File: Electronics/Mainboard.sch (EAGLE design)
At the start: 35 parts, among them IC1 4081N, IC2 4069N, Q1 IRFZ48V, Q2 IRF4905V, Q3 IRFZ48V, Q4 IRF4905V, Q5 IRFZ48V, Q6 IRF4905V, Q7 IRFZ48V, Q8 IRF4905V, X3 24V Batt

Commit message: Arduino sofware, updated electronics and some report outline.
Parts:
- removed C1: (no value), rcl:CPOL-EUE7.5-18
- added C2: (no value), rcl:CPOL-EUE5-10.5
- added LED1: (no value), led:LED5MM
- added R13: 1k, rcl:R-EU_0207/10
- R10, R11, R12, R7, R8, R9: value (none) -> 180
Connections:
- net N$35 renamed +3V3
- removed net N$29: C1.-, OK1.EMIT, OK2.EMIT, OK3.EMIT, OK4.EMIT, OK5.EMIT, OK6.EMIT, Q1.S, Q3.S, Q5.S, Q7.S, X3-2.KL
- removed net N$30: C1.+, Q2.S, Q4.S, Q6.S, Q8.S, R1.2, R2.2, R3.2, R4.2, R5.2, R6.2, X3-1.KL
- new net +24V: C2.+, LED1.A, Q2.S, Q4.S, Q6.S, Q8.S, R1.2, R2.2, R3.2, R4.2, R5.2, R6.2, X3-1.KL
- new net GND2: C2.-, OK1.EMIT, OK2.EMIT, OK3.EMIT, OK4.EMIT, OK5.EMIT, OK6.EMIT, Q1.S, Q3.S, Q5.S, Q7.S, R13.1, X3-2.KL
- new net N$41: JP1.3
- new net N$42: JP1.4
- new net N$6: LED1.C, R13.2
- net N$26: no longer JP1.4
- net N$37: no longer JP1.3
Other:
- note added: "Beskyttelses dioder?"
- note added: "Level Shifter"
- moved on the sheet: JP1, X3-1, X3-2

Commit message: 
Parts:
- removed C2: (no value), rcl:CPOL-EUE5-10.5
- removed IC2: 4069N, 40xx:4069N
- removed LED1: (no value), led:LED5MM
- removed OK1, OK2, OK3, OK4, OK5, OK6: PC817, optocoupler:PC817
- removed Q1, Q3, Q5, Q7: IRFZ48V, transistor-power:IRFZ48V
- removed Q2, Q4, Q6, Q8: IRF4905V, transistor-power:IRF4905V
- removed R1, R2, R3, R4, R5, R6: 10k, rcl:R-EU_0207/10
- removed R11, R12: 180, rcl:R-EU_0207/10
- removed R13: 1k, rcl:R-EU_0207/10
- removed X1, X2: (no value), con-wago-508:W237-02P
- removed X3: 24V Batt, con-wago-508:W237-02P
- added JP2: Motorcontroller, pinhead:PINHD-2X5
- added JP5: Display, pinhead:PINHD-2X7
- added T1, T2: BC547, transistor:BC547
- JP1: device pinhead:PINHD-1X6 -> pinhead:PINHD-2X7
- R10, R9: value 180 -> 1k
- R7, R8: value 180 -> 10k
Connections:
- removed net +24V: C2.+, LED1.A, Q2.S, Q4.S, Q6.S, Q8.S, R1.2, R2.2, R3.2, R4.2, R5.2, R6.2, X3-1.KL
- removed net GND2: C2.-, OK1.EMIT, OK2.EMIT, OK3.EMIT, OK4.EMIT, OK5.EMIT, OK6.EMIT, Q1.S, Q3.S, Q5.S, Q7.S, R13.1, X3-2.KL
- removed net N$12: OK1.COL, Q1.G, Q2.G, R1.1
- removed net N$13: OK3.COL, Q3.G, R3.1
- removed net N$14: OK3.A, R9.2
- removed net N$15: IC1A.O, R8.1
- removed net N$18: Q7.D, Q8.D, X2-1.KL
- removed net N$19: OK4.COL, Q7.G, Q8.G, R4.1
- removed net N$21: OK5.COL, Q6.G, R5.1
- removed net N$22: OK6.COL, Q5.G, R6.1
- removed net N$23: OK6.A, R12.2
- removed net N$24: IC1C.O, R11.1
- removed net N$25: IC1D.O, R12.1
- removed net N$27: IC1D.I0, IC2B.I, R10.1, U$1.D4
- removed net N$28: OK1.A, R7.2
- removed net N$6: LED1.C, R13.2
- removed net N$9: OK2.COL, Q4.G, R2.1
- removed net VCC: IC1P.VDD, IC2P.VDD, U$1.5V
- new net +5V: IC1P.VDD, JP5.2, R7.2, R8.2, U$1.5V
- new net N$31: JP5.4, U$1.D6
- new net N$38: JP5.8, U$1.D8
- new net N$40: JP5.10, U$1.D9
- new net N$43: JP5.14, U$1.D11
- new net N$44: JP5.3, U$1.D12
- new net N$45: JP5.5, U$1.D13
- new net N$46: JP5.7, U$1.A3
- net GND: now also JP1.3, JP2.10, JP5.1, T1.E, T2.E; no longer IC2P.VSS, JP1.2, OK1.C, OK2.C, OK3.C, OK4.C, OK5.C, OK6.C
- net N$1: now also IC1A.O, JP2.2; no longer Q5.D, Q6.D, X2-2.KL
- net N$10: now also JP2.1, R9.1; no longer IC2A.I, R7.1
- net N$16: now also R8.1, T2.C; no longer IC2B.O
- net N$17: now also R9.2, T1.B; no longer IC1B.O, R9.1
- net N$2: now also IC1B.O, JP2.3; no longer Q3.D, Q4.D, X1-1.KL
- net N$20: now also R10.2, T2.B; no longer OK5.A, R11.2
- net N$26: now also JP1.7
- net N$3: now also IC1D.I0, JP2.4, R10.1, U$1.D4; no longer OK2.A, R8.2
- net N$37: now also JP5.6, U$1.D7; no longer U$1.A4
- net N$4: now also IC1C.O, JP2.5; no longer Q1.D, Q2.D, X1-2.KL
- net N$41: now also JP1.5, U$1.A4; no longer JP1.3
- net N$42: now also JP5.12, U$1.D10; no longer JP1.4
- net N$5: now also IC1D.O, JP2.6; no longer OK4.A, R10.2
- net N$8: now also R7.1, T1.C; no longer IC2A.O
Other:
- note removed: "Beskyttelses dioder?"
- note removed: "Level Shifter"
- moved on the sheet: IC1A, IC1B, IC1C, IC1D, IC1P, R10, R7, R8, R9

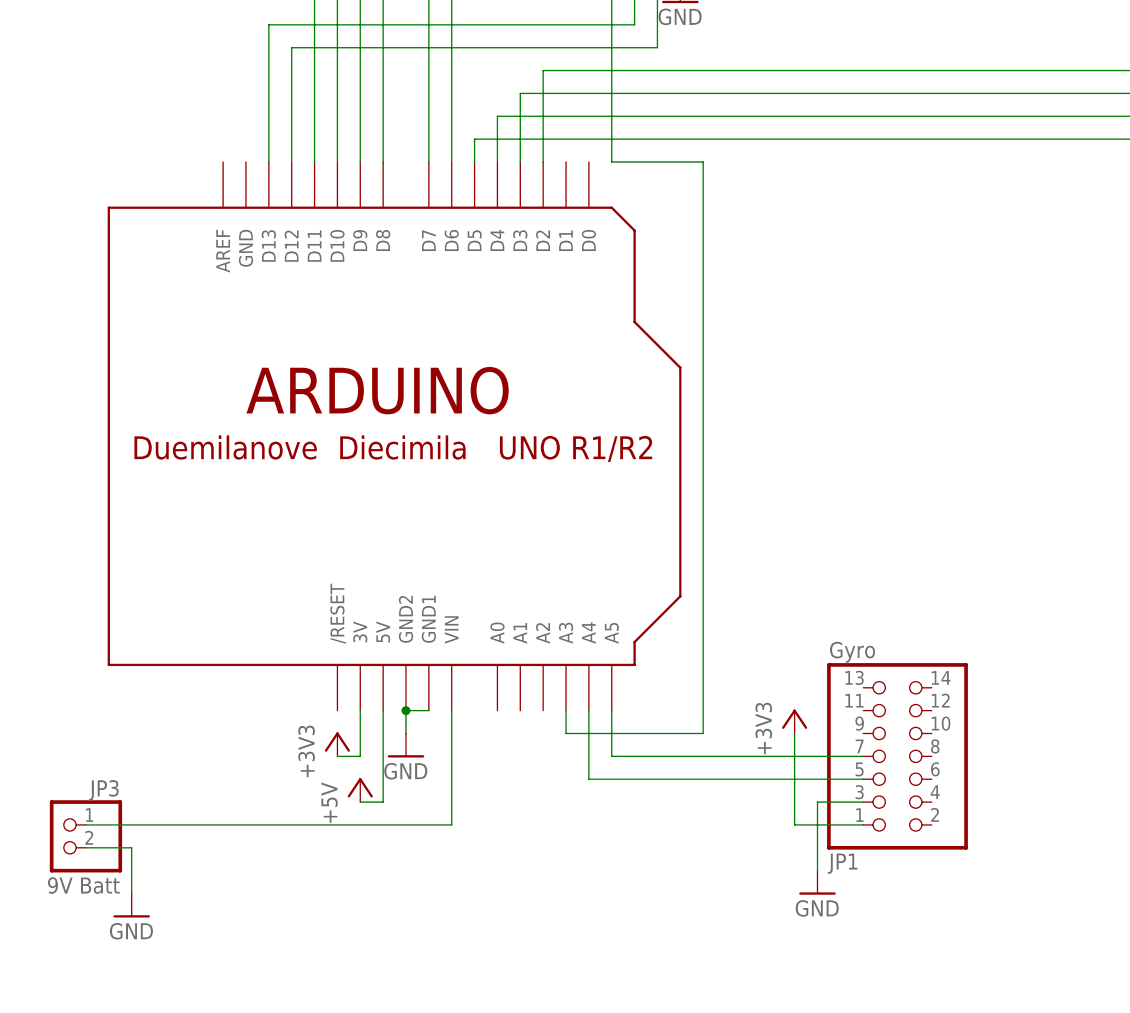
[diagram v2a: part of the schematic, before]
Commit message: Mainboard 2.0. Fixes #1, #2 #12
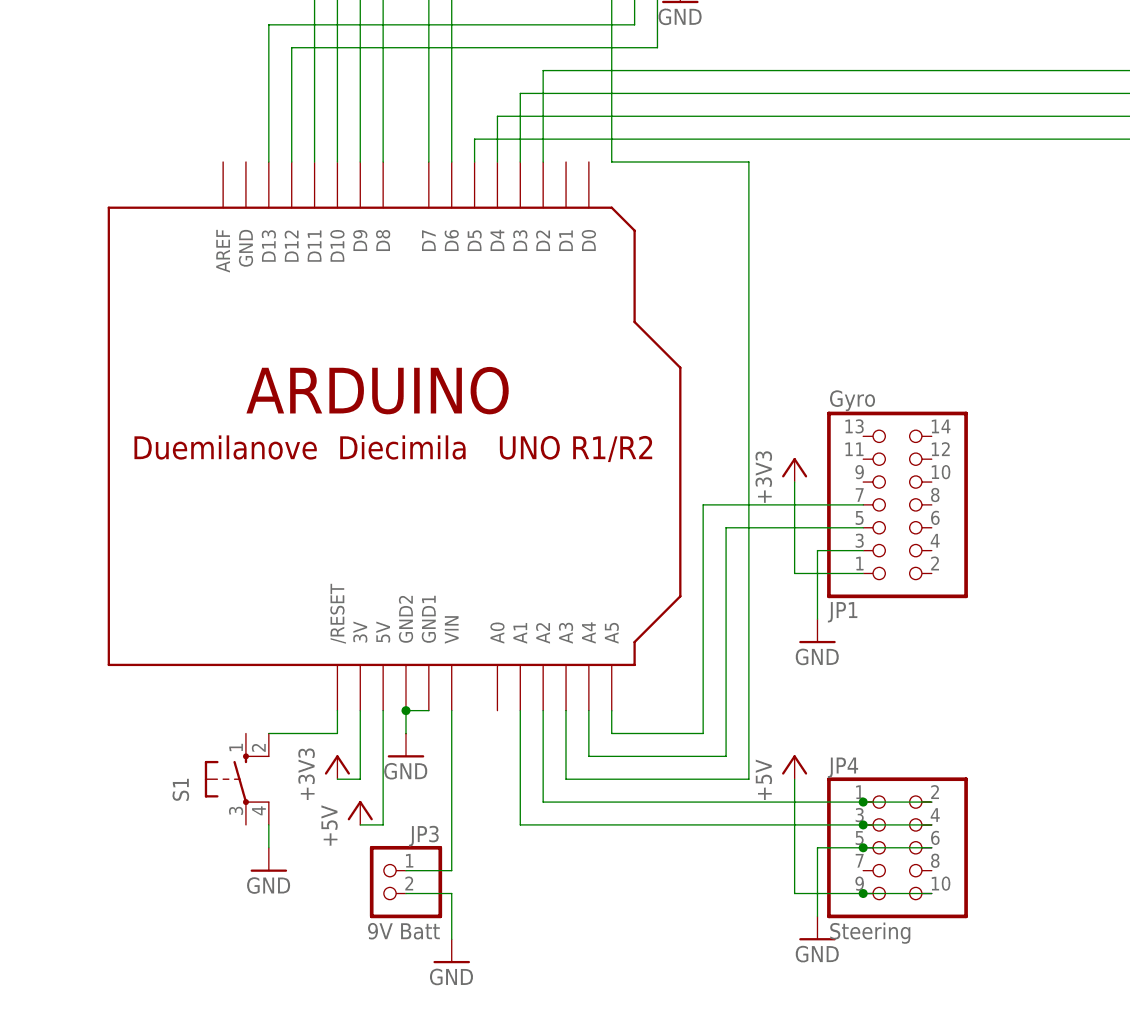
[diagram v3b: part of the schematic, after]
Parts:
- added JP4: Steering, pinhead:PINHD-2X5
- added S1: (no value), switch-omron:10-XX
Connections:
- new net N$13: JP4.3, JP4.4, U$1.A1
- new net N$14: JP4.1, JP4.2, U$1.A2
- new net N$15: S1.S1, U$1./RESET
- net +5V: now also JP4.10, JP4.9
- net GND: now also JP4.5, JP4.6, S1.P1
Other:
- moved on the sheet: JP1, JP3
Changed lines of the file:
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@@
 <?xml version="1.0" encoding="utf-8"?>
 <!DOCTYPE eagle SYSTEM "eagle.dtd">
-<eagle version="6.0">
+<eagle version="6.1">
 <drawing>
 <settings>
@@
 <part name="P+4" library="supply1" deviceset="+5V" device=""/>
 <part name="P+5" library="supply1" deviceset="+5V" device=""/>
+<part name="GND9" library="supply1" deviceset="GND" device=""/>
+<part name="P+6" library="supply1" deviceset="+5V" device=""/>
+<part name="JP4" library="pinhead" deviceset="PINHD-2X5" device="" value="Steering"/>
+<part name="S1" library="switch-omron" deviceset="10-XX" device=""/>
+<part name="GND10" library="supply1" deviceset="GND" device=""/>
 </parts>
 <sheets>
@@
 <instance part="IC1" gate="C" x="132.08" y="55.88"/>
 <instance part="IC1" gate="D" x="132.08" y="40.64"/>
-<instance part="JP1" gate="A" x="53.34" y="35.56" rot="MR180"/>
-<instance part="JP3" gate="G$1" x="-38.1" y="25.4" rot="MR0"/>
-<instance part="GND1" gate="1" x="-30.48" y="17.78"/>
-<instance part="GND2" gate="1" x="45.72" y="20.32"/>
+<instance part="JP1" gate="A" x="53.34" y="63.5" rot="MR180"/>
+<instance part="JP3" gate="G$1" x="-2.54" y="20.32" rot="MR0"/>
+<instance part="GND1" gate="1" x="5.08" y="12.7"/>
+<instance part="GND2" gate="1" x="45.72" y="48.26"/>
 <instance part="GND3" gate="1" x="0" y="35.56"/>
 <instance part="GND4" gate="1" x="91.44" y="27.94"/>
 <instance part="GND6" gate="1" x="162.56" y="68.58"/>
-<instance part="+3V1" gate="G$1" x="-7.62" y="38.1"/>
-<instance part="+3V2" gate="G$1" x="43.18" y="40.64"/>
+<instance part="+3V1" gate="G$1" x="-7.62" y="35.56"/>
+<instance part="+3V2" gate="G$1" x="43.18" y="68.58"/>
 <instance part="T1" gate="G$1" x="119.38" y="111.76"/>
 <instance part="T2" gate="G$1" x="116.84" y="58.42"/>
@@
 <instance part="P+3" gate="1" x="137.16" y="121.92"/>
 <instance part="P+4" gate="1" x="137.16" y="68.58"/>
-<instance part="P+5" gate="1" x="-5.08" y="33.02"/>
+<instance part="P+5" gate="1" x="-5.08" y="30.48"/>
+<instance part="GND9" gate="1" x="45.72" y="15.24"/>
+<instance part="P+6" gate="1" x="43.18" y="35.56"/>
+<instance part="JP4" gate="A" x="53.34" y="25.4"/>
+<instance part="S1" gate="1" x="-17.78" y="33.02"/>
+<instance part="GND10" gate="1" x="-15.24" y="22.86"/>
 </instances>
 <busses>
@@
 <segment>
 <pinref part="U$1" gate="G$1" pin="VIN"/>
-<wire x1="5.08" y1="40.64" x2="5.08" y2="27.94" width="0.1524" layer="91"/>
-<wire x1="5.08" y1="27.94" x2="-35.56" y2="27.94" width="0.1524" layer="91"/>
+<wire x1="5.08" y1="40.64" x2="5.08" y2="22.86" width="0.1524" layer="91"/>
+<wire x1="5.08" y1="22.86" x2="0" y2="22.86" width="0.1524" layer="91"/>
 <pinref part="JP3" gate="G$1" pin="1"/>
 </segment>
@@
 <pinref part="GND1" gate="1" pin="GND"/>
 <pinref part="JP3" gate="G$1" pin="2"/>
-<wire x1="-35.56" y1="25.4" x2="-30.48" y2="25.4" width="0.1524" layer="91"/>
-<wire x1="-30.48" y1="25.4" x2="-30.48" y2="20.32" width="0.1524" layer="91"/>
+<wire x1="0" y1="20.32" x2="5.08" y2="20.32" width="0.1524" layer="91"/>
+<wire x1="5.08" y1="20.32" x2="5.08" y2="15.24" width="0.1524" layer="91"/>
 </segment>
 <segment>
 <pinref part="JP1" gate="A" pin="3"/>
-<wire x1="50.8" y1="30.48" x2="45.72" y2="30.48" width="0.1524" layer="91"/>
-<wire x1="45.72" y1="30.48" x2="45.72" y2="22.86" width="0.1524" layer="91"/>
+<wire x1="50.8" y1="58.42" x2="45.72" y2="58.42" width="0.1524" layer="91"/>
+<wire x1="45.72" y1="58.42" x2="45.72" y2="50.8" width="0.1524" layer="91"/>
 <pinref part="GND2" gate="1" pin="GND"/>
 </segment>
@@
 <wire x1="30.48" y1="121.92" x2="30.48" y2="127" width="0.1524" layer="91"/>
 </segment>
+<segment>
+<wire x1="45.72" y1="25.4" x2="45.72" y2="17.78" width="0.1524" layer="91"/>
+<pinref part="GND9" gate="1" pin="GND"/>
+<pinref part="JP4" gate="A" pin="5"/>
+<wire x1="45.72" y1="25.4" x2="50.8" y2="25.4" width="0.1524" layer="91"/>
+<pinref part="JP4" gate="A" pin="6"/>
+<wire x1="50.8" y1="25.4" x2="58.42" y2="25.4" width="0.1524" layer="91"/>
+<junction x="50.8" y="25.4"/>
+</segment>
+<segment>
+<pinref part="GND10" gate="1" pin="GND"/>
+<pinref part="S1" gate="1" pin="P1"/>
+<wire x1="-15.24" y1="25.4" x2="-15.24" y2="27.94" width="0.1524" layer="91"/>
+</segment>
 </net>
 <net name="N$26" class="0">
 <segment>
 <pinref part="U$1" gate="G$1" pin="A5"/>
-<wire x1="22.86" y1="40.64" x2="22.86" y2="35.56" width="0.1524" layer="91"/>
+<wire x1="22.86" y1="40.64" x2="22.86" y2="38.1" width="0.1524" layer="91"/>
 <pinref part="JP1" gate="A" pin="7"/>
-<wire x1="50.8" y1="35.56" x2="22.86" y2="35.56" width="0.1524" layer="91"/>
+<wire x1="50.8" y1="63.5" x2="33.02" y2="63.5" width="0.1524" layer="91"/>
+<wire x1="33.02" y1="63.5" x2="33.02" y2="38.1" width="0.1524" layer="91"/>
+<wire x1="33.02" y1="38.1" x2="22.86" y2="38.1" width="0.1524" layer="91"/>
 </segment>
 </net>
@@
 <segment>
 <pinref part="JP1" gate="A" pin="5"/>
-<wire x1="50.8" y1="33.02" x2="20.32" y2="33.02" width="0.1524" layer="91"/>
+<wire x1="50.8" y1="60.96" x2="35.56" y2="60.96" width="0.1524" layer="91"/>
+<wire x1="35.56" y1="60.96" x2="35.56" y2="35.56" width="0.1524" layer="91"/>
+<wire x1="35.56" y1="35.56" x2="20.32" y2="35.56" width="0.1524" layer="91"/>
 <pinref part="U$1" gate="G$1" pin="A4"/>
-<wire x1="20.32" y1="33.02" x2="20.32" y2="40.64" width="0.1524" layer="91"/>
+<wire x1="20.32" y1="35.56" x2="20.32" y2="40.64" width="0.1524" layer="91"/>
 </segment>
 </net>
@@
 <segment>
 <pinref part="U$1" gate="G$1" pin="3V"/>
-<wire x1="-5.08" y1="40.64" x2="-5.08" y2="35.56" width="0.1524" layer="91"/>
+<wire x1="-5.08" y1="40.64" x2="-5.08" y2="33.02" width="0.1524" layer="91"/>
 <pinref part="+3V1" gate="G$1" pin="+3V3"/>
-<wire x1="-5.08" y1="35.56" x2="-7.62" y2="35.56" width="0.1524" layer="91"/>
+<wire x1="-5.08" y1="33.02" x2="-7.62" y2="33.02" width="0.1524" layer="91"/>
 </segment>
 <segment>
 <pinref part="JP1" gate="A" pin="1"/>
 <pinref part="+3V2" gate="G$1" pin="+3V3"/>
-<wire x1="50.8" y1="27.94" x2="43.18" y2="27.94" width="0.1524" layer="91"/>
-<wire x1="43.18" y1="27.94" x2="43.18" y2="38.1" width="0.1524" layer="91"/>
+<wire x1="50.8" y1="55.88" x2="43.18" y2="55.88" width="0.1524" layer="91"/>
+<wire x1="43.18" y1="55.88" x2="43.18" y2="66.04" width="0.1524" layer="91"/>
 </segment>
 </net>
@@
 <pinref part="JP5" gate="A" pin="7"/>
 <wire x1="22.86" y1="127" x2="22.86" y2="101.6" width="0.1524" layer="91"/>
-<wire x1="22.86" y1="101.6" x2="33.02" y2="101.6" width="0.1524" layer="91"/>
-<wire x1="33.02" y1="101.6" x2="33.02" y2="38.1" width="0.1524" layer="91"/>
-<wire x1="33.02" y1="38.1" x2="17.78" y2="38.1" width="0.1524" layer="91"/>
+<wire x1="22.86" y1="101.6" x2="38.1" y2="101.6" width="0.1524" layer="91"/>
+<wire x1="38.1" y1="101.6" x2="38.1" y2="33.02" width="0.1524" layer="91"/>
+<wire x1="38.1" y1="33.02" x2="17.78" y2="33.02" width="0.1524" layer="91"/>
 <pinref part="U$1" gate="G$1" pin="A3"/>
-<wire x1="17.78" y1="38.1" x2="17.78" y2="40.64" width="0.1524" layer="91"/>
+<wire x1="17.78" y1="33.02" x2="17.78" y2="40.64" width="0.1524" layer="91"/>
 </segment>
 </net>
@@
 <segment>
 <pinref part="U$1" gate="G$1" pin="5V"/>
-<wire x1="-2.54" y1="40.64" x2="-2.54" y2="30.48" width="0.1524" layer="91"/>
+<wire x1="-2.54" y1="40.64" x2="-2.54" y2="27.94" width="0.1524" layer="91"/>
 <pinref part="P+5" gate="1" pin="+5V"/>
-<wire x1="-2.54" y1="30.48" x2="-5.08" y2="30.48" width="0.1524" layer="91"/>
+<wire x1="-2.54" y1="27.94" x2="-5.08" y2="27.94" width="0.1524" layer="91"/>
 </segment>
 <segment>
@@
 <wire x1="137.16" y1="116.84" x2="137.16" y2="119.38" width="0.1524" layer="91"/>
 </segment>
-</net>
+<segment>
+<wire x1="43.18" y1="20.32" x2="43.18" y2="33.02" width="0.1524" layer="91"/>
+<pinref part="P+6" gate="1" pin="+5V"/>
+<pinref part="JP4" gate="A" pin="9"/>
+<wire x1="43.18" y1="20.32" x2="50.8" y2="20.32" width="0.1524" layer="91"/>
+<pinref part="JP4" gate="A" pin="10"/>
+<wire x1="50.8" y1="20.32" x2="58.42" y2="20.32" width="0.1524" layer="91"/>
+<junction x="50.8" y="20.32"/>
+</segment>
+</net>
+<net name="N$13" class="0">
+<segment>
+<pinref part="JP4" gate="A" pin="3"/>
+<pinref part="U$1" gate="G$1" pin="A1"/>
+<wire x1="50.8" y1="27.94" x2="12.7" y2="27.94" width="0.1524" layer="91"/>
+<wire x1="12.7" y1="27.94" x2="12.7" y2="40.64" width="0.1524" layer="91"/>
+<pinref part="JP4" gate="A" pin="4"/>
+<wire x1="50.8" y1="27.94" x2="58.42" y2="27.94" width="0.1524" layer="91"/>
+<junction x="50.8" y="27.94"/>
+</segment>
+</net>
+<net name="N$14" class="0">
+<segment>
+<pinref part="JP4" gate="A" pin="2"/>
+<pinref part="JP4" gate="A" pin="1"/>
+<wire x1="58.42" y1="30.48" x2="50.8" y2="30.48" width="0.1524" layer="91"/>
+<pinref part="U$1" gate="G$1" pin="A2"/>
+<wire x1="15.24" y1="40.64" x2="15.24" y2="30.48" width="0.1524" layer="91"/>
+<wire x1="15.24" y1="30.48" x2="50.8" y2="30.48" width="0.1524" layer="91"/>
+<junction x="50.8" y="30.48"/>
+</segment>
+</net>
+<net name="N$15" class="0">
+<segment>
+<pinref part="U$1" gate="G$1" pin="/RESET"/>
+<wire x1="-7.62" y1="40.64" x2="-7.62" y2="38.1" width="0.1524" layer="91"/>
+<pinref part="S1" gate="1" pin="S1"/>
+<wire x1="-7.62" y1="38.1" x2="-15.24" y2="38.1" width="0.1524" layer="91"/>
+</segment>
+</net>
